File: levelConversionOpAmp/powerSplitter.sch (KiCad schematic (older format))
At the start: 11 parts, among them Q1 PN2222A, Q2 PN2222A, U1 TL082

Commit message: Placement des composantes sur plaque perforee
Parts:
- Q1, Q2: footprint Package_TO_SOT_THT:TO-92_Inline -> Package_TO_SOT_THT:TO-92_Inline_Wide
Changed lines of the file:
@@
 F 0 "Q1" H 5640 3596 50  0000 L CNN
 F 1 "PN2222A" H 5640 3505 50  0000 L CNN
-F 2 "Package_TO_SOT_THT:TO-92_Inline" H 5650 3475 50  0001 L CIN
+F 2 "Package_TO_SOT_THT:TO-92_Inline_Wide" H 5650 3475 50  0001 L CIN
 F 3 "https://www.onsemi.com/pub/Collateral/PN2222-D.PDF" H 5450 3550 50  0001 L CNN
 	1    5450 3550
@@
 F 0 "Q2" H 7890 3846 50  0000 L CNN
 F 1 "PN2222A" H 7890 3755 50  0000 L CNN
-F 2 "Package_TO_SOT_THT:TO-92_Inline" H 7900 3725 50  0001 L CIN
+F 2 "Package_TO_SOT_THT:TO-92_Inline_Wide" H 7900 3725 50  0001 L CIN
 F 3 "https://www.onsemi.com/pub/Collateral/PN2222-D.PDF" H 7700 3800 50  0001 L CNN
 	1    7700 3800

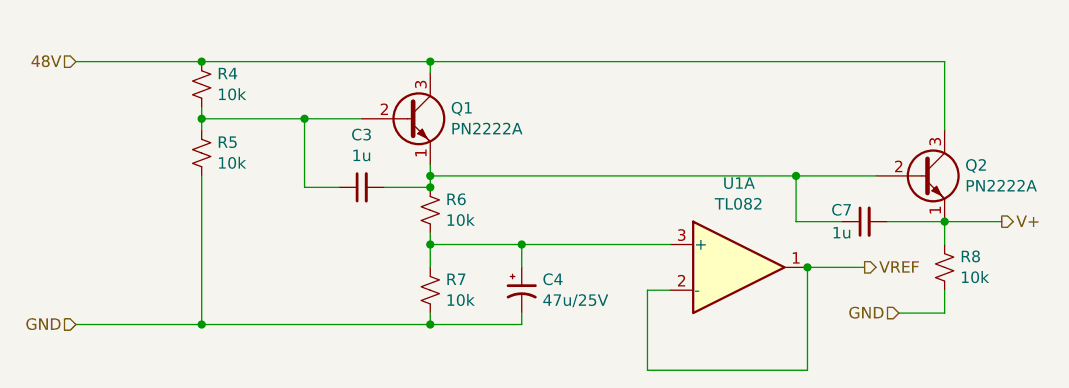
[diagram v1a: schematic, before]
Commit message: Changed layout a little. Added ground bias resistor at output to quickly set output DC level even when plugged into a high impedance load
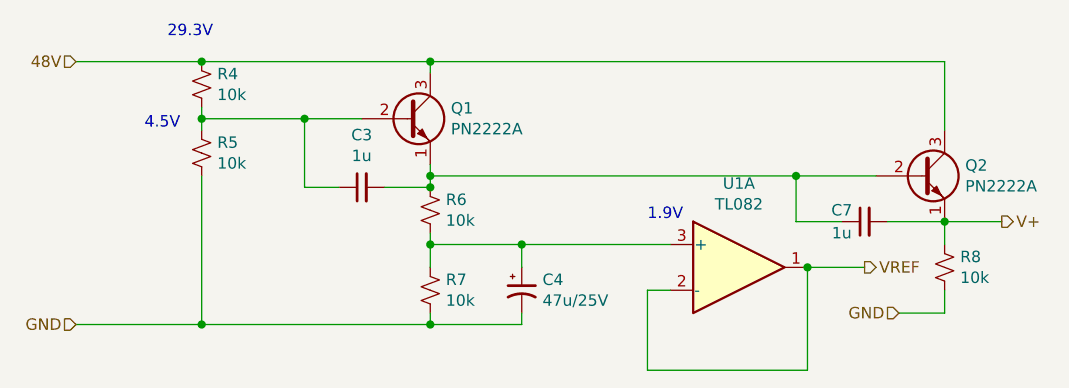
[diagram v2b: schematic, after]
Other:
- note added: "1.9V"
- note added: "29.3V"
- note added: "4.5V"
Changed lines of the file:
@@
 	5350 3850 5550 3850
 Connection ~ 5550 3850
+Text Notes 6500 4000 0    50   ~ 0
+1.9V
+Text Notes 4300 3600 0    50   ~ 0
+4.5V
+Text Notes 4400 3200 0    50   ~ 0
+29.3V
 $EndSCHEMATC
